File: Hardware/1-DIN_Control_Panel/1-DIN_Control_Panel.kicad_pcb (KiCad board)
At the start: 2 copper layers, 177.8 x 50.8 mm, 0 parts

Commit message: Schematic progress
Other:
- outline, holes or cut-outs redrawn
- board text added: "1"
- board text added: "2"
- board text added: "3"
- board text added: "4"
- board text added: "5"
- board text added: "6"
- board text added: "7"
- board text added: "AMP"
- board text added: "AUX JUMP"
- board text added: "BATT BYPASS"
- board text added: "BRT"
- board text added: "MASTER"
- board text added: "MODE"
- board text added: "OFF"
- board text added: "ON"
- board text added: "VOLT"

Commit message: Assigned footprints, expanded schematic
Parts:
- added A1: Arduino Nano, Module:Arduino_Nano, F.Cu at (-5.53, 52.9)
- added C1: 100nF, Capacitor_SMD:C_0603_1608Metric_Pad1.08x0.95mm_HandSolder, F.Cu at (-5.41, 107.6)
- added C2: 100nF, Capacitor_SMD:C_0603_1608Metric_Pad1.08x0.95mm_HandSolder, F.Cu at (-5.41, 110.2)
- added C3: 100nF, Capacitor_SMD:C_0603_1608Metric_Pad1.08x0.95mm_HandSolder, F.Cu at (-5.41, 112.7)
- added C4: 100nF, Capacitor_SMD:C_0603_1608Metric_Pad1.08x0.95mm_HandSolder, F.Cu at (-5.41, 115.2)
- added C5: DNP, Capacitor_SMD:C_0603_1608Metric_Pad1.08x0.95mm_HandSolder, F.Cu at (-5.41, 117.7)
- added C6: DNP, Capacitor_SMD:C_0603_1608Metric_Pad1.08x0.95mm_HandSolder, F.Cu at (-5.41, 120.2)
- added C7: 10µF, Capacitor_SMD:C_0603_1608Metric_Pad1.08x0.95mm_HandSolder, F.Cu at (-5.41, 122.7)
- added C8: 22µF, Capacitor_SMD:C_0603_1608Metric_Pad1.08x0.95mm_HandSolder, F.Cu at (-5.41, 125.2)
- added C9: 100nF, Capacitor_SMD:C_0603_1608Metric_Pad1.08x0.95mm_HandSolder, F.Cu at (-1.06, 107.6)
- added D1: D, Diode_THT:D_A-405_P2.54mm_Vertical_AnodeUp, F.Cu at (24.7, 58.7)
- added D2: D, Diode_THT:D_A-405_P2.54mm_Vertical_AnodeUp, F.Cu at (24.7, 62.9)
- added D3: D, Diode_THT:D_A-405_P2.54mm_Vertical_AnodeUp, F.Cu at (24.7, 67.2)
- added J1: 2x05 Molex Micro-Fit 3.0 43045, Connector_Molex:Molex_Micro-Fit_3.0_43045-1012_2x05_P3.00mm_Vertical, F.Cu at (16.4, 83.9)
- added J2: Pot/SW - Brightness, TerminalBlock:TerminalBlock_bornier-5_P5.08mm, F.Cu at (8.73, 122.7)
- added J3: SW - Aux Jump-Start, Connector_Molex:Molex_Micro-Fit_3.0_43045-0212_2x01_P3.00mm_Vertical, F.Cu at (-2.98, 99.0)
- added J4: SW - Battery Bypass, Connector_Molex:Molex_Micro-Fit_3.0_43045-0212_2x01_P3.00mm_Vertical, F.Cu at (6.23, 99.0)
- added J5: SW - Master Power, Connector_Molex:Molex_Micro-Fit_3.0_43045-0212_2x01_P3.00mm_Vertical, F.Cu at (15.4, 99.0)
- added K1: FINDER-40.52, Relay_THT:Relay_DPDT_Finder_30.22, F.Cu at (7.64, 116.0)
- added R1: DNP, Resistor_SMD:R_0603_1608Metric_Pad0.98x0.95mm_HandSolder, F.Cu at (-1.06, 110.2)
- added R10: 100kΩ, Resistor_SMD:R_0603_1608Metric_Pad0.98x0.95mm_HandSolder, F.Cu at (3.29, 112.7)
- added R11: 100kΩ, Resistor_SMD:R_0603_1608Metric_Pad0.98x0.95mm_HandSolder, F.Cu at (3.29, 115.2)
- added R12: 100kΩ, Resistor_SMD:R_0603_1608Metric_Pad0.98x0.95mm_HandSolder, F.Cu at (3.29, 117.7)
- added R2: DNP, Resistor_SMD:R_0603_1608Metric_Pad0.98x0.95mm_HandSolder, F.Cu at (-1.06, 112.7)
- added R3: 12kΩ, Resistor_SMD:R_0603_1608Metric_Pad0.98x0.95mm_HandSolder, F.Cu at (-1.06, 115.2)
- added R4: 22kΩ, Resistor_SMD:R_0603_1608Metric_Pad0.98x0.95mm_HandSolder, F.Cu at (-1.06, 117.7)
- added R5: 10kΩ, Resistor_SMD:R_0603_1608Metric_Pad0.98x0.95mm_HandSolder, F.Cu at (-1.06, 120.2)
- added R6: 100kΩ, Resistor_SMD:R_0603_1608Metric_Pad0.98x0.95mm_HandSolder, F.Cu at (-1.06, 122.7)
- added R7: 2.7kΩ, Resistor_SMD:R_0603_1608Metric_Pad0.98x0.95mm_HandSolder, F.Cu at (-1.06, 125.2)
- added R8: 100kΩ, Resistor_SMD:R_0603_1608Metric_Pad0.98x0.95mm_HandSolder, F.Cu at (3.29, 107.6)
- added R9: 100kΩ, Resistor_SMD:R_0603_1608Metric_Pad0.98x0.95mm_HandSolder, F.Cu at (3.29, 110.2)
- added RV1: 500Ω, Buzzer_Beeper:Buzzer_12x9.5RM7.6, F.Cu at (-48.7, 138.3)
- added U1: D198K, Display_7Segment:D1X8K, F.Cu at (-25.5, 50.2)
- added U2: D198K, Display_7Segment:D1X8K, F.Cu at (-25.5, 64.3)
- added U3: D198K, Display_7Segment:D1X8K, F.Cu at (-25.5, 78.3)
- added U4: D198K, Display_7Segment:D1X8K, F.Cu at (-25.5, 92.4)
- added U5: D198K, Display_7Segment:D1X8K, F.Cu at (-25.5, 106.4)
- added U6: D198K, Display_7Segment:D1X8K, F.Cu at (-25.5, 120.5)
- added U7: MAX7221xNG, Package_DIP:DIP-24_W7.62mm, F.Cu at (13.4, 50.4)
- added U8: LM324DR, Package_SO:SOIC-14_3.9x8.7mm_P1.27mm, F.Cu at (24.3, 100.7)
- added U9: AP1117-50, Package_TO_SOT_SMD:SOT-223-3_TabPin2, F.Cu at (27.5, 52.4)
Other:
- board size 177.8 x 50.8 mm -> 221.3 x 154.1 mm
- board text added: "PUSH TO TEST"

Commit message: Changed to 14-segement Characters
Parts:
- U7: footprint Package_DIP:DIP-24_W7.62mm -> Package_DIP:DIP-24_W8.89mm_SMDSocket_LongPads
- moved A1 54.2 mm to (48.2, 59.9)
- moved U7 15.1 mm to (17.7, 64.8)
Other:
- board size 221.3 x 154.1 mm -> 177.8 x 130.7 mm

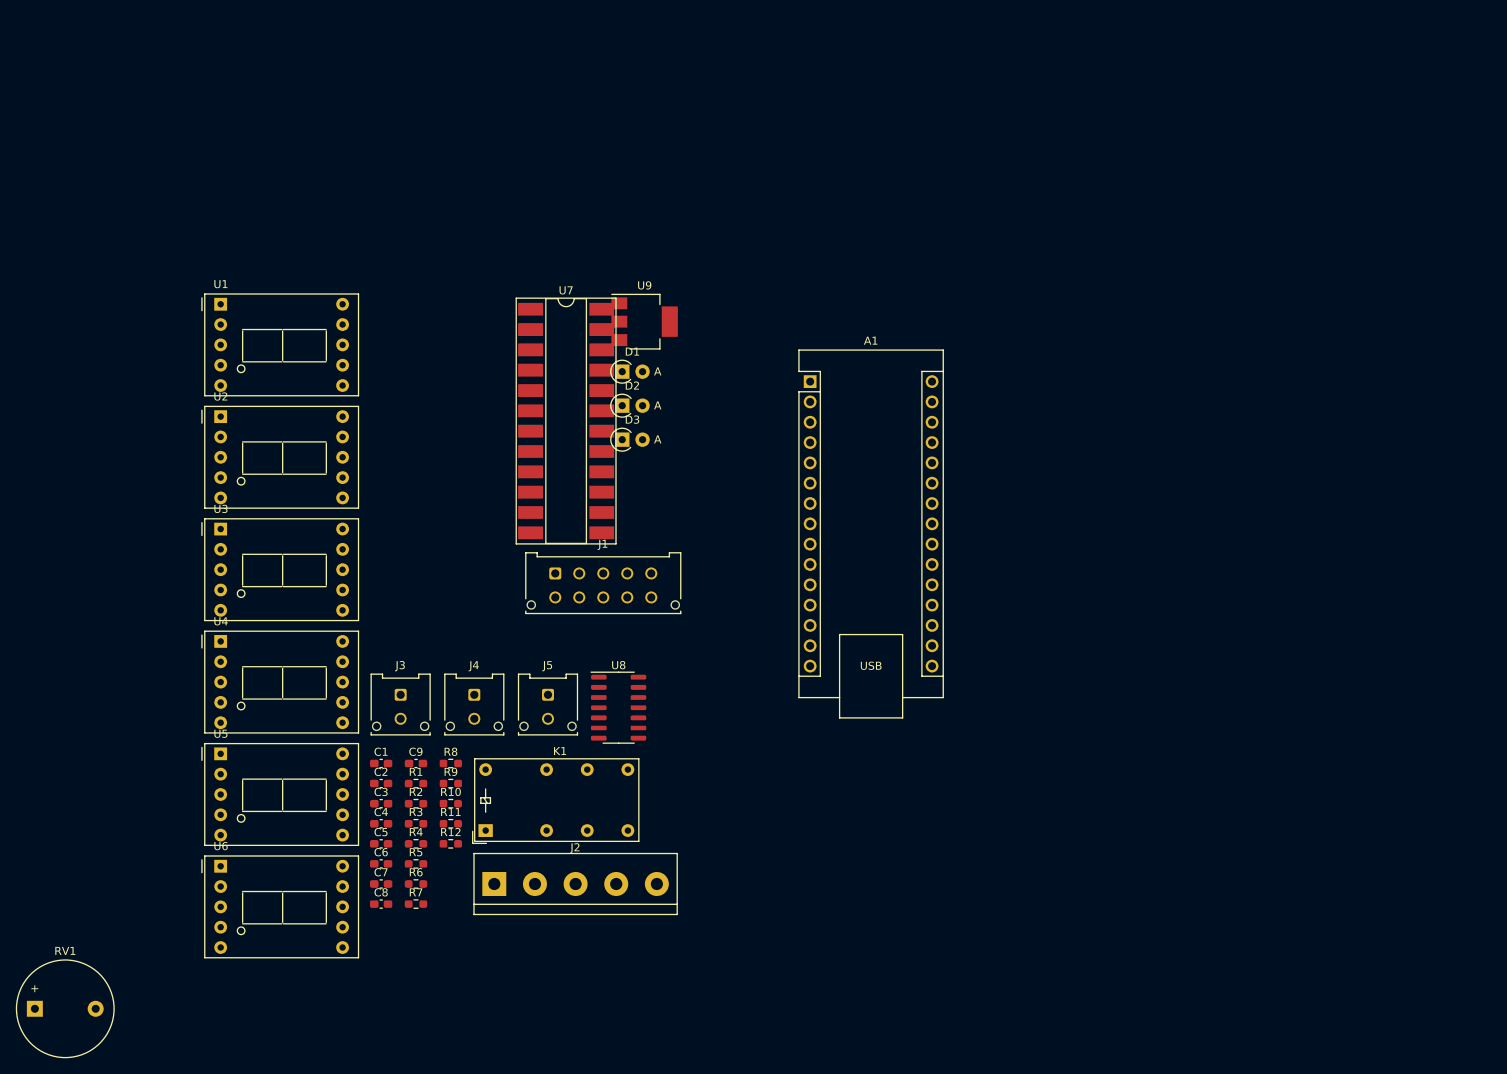
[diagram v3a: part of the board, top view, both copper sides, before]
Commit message: Added footprints to pcb file
Need a proper footprint for the 14-seg LEDs, MAX driver chips...and something else that I can't remember right now
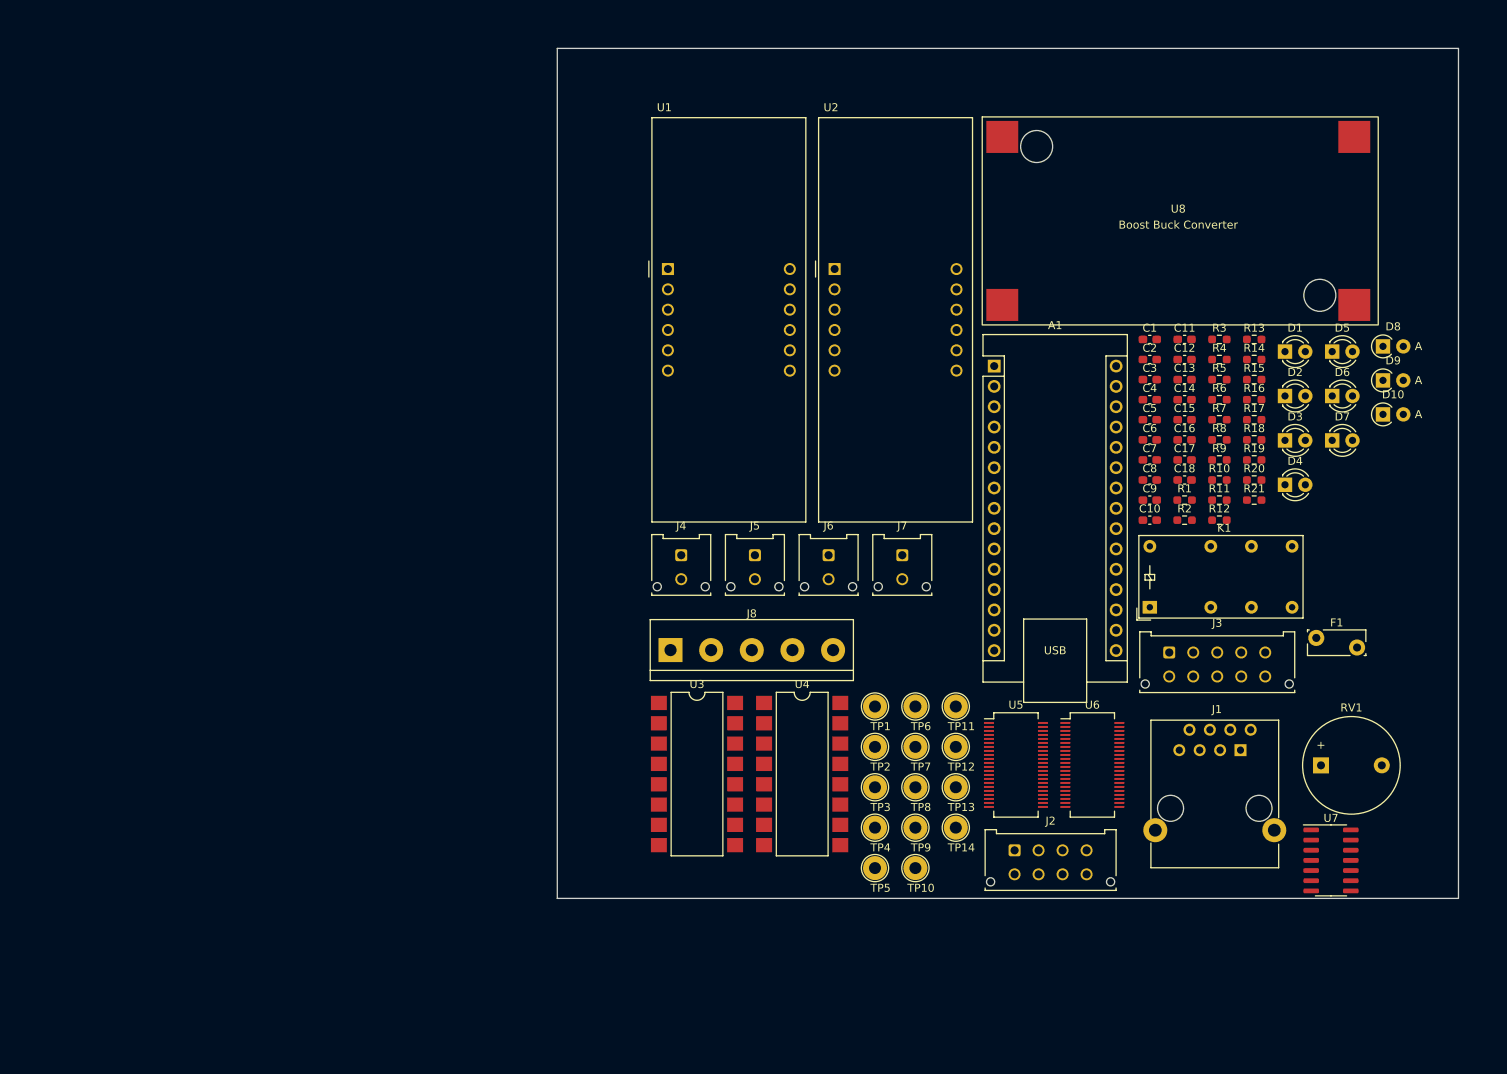
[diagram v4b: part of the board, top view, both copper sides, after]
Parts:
- removed U9: AP1117-50, Package_TO_SOT_SMD:SOT-223-3_TabPin2
- added C10: 100nF, Capacitor_SMD:C_0603_1608Metric_Pad1.08x0.95mm_HandSolder, F.Cu at (90.7, 77.2)
- added C11: 100nF, Capacitor_SMD:C_0603_1608Metric_Pad1.08x0.95mm_HandSolder, F.Cu at (95.0, 54.6)
- added C12: 100nF, Capacitor_SMD:C_0603_1608Metric_Pad1.08x0.95mm_HandSolder, F.Cu at (95.0, 57.1)
- added C13: 100nF, Capacitor_SMD:C_0603_1608Metric_Pad1.08x0.95mm_HandSolder, F.Cu at (95.0, 59.6)
- added C14: 100nF, Capacitor_SMD:C_0603_1608Metric_Pad1.08x0.95mm_HandSolder, F.Cu at (95.0, 62.2)
- added C15: 10µF, Capacitor_SMD:C_0603_1608Metric_Pad1.08x0.95mm_HandSolder, F.Cu at (95.0, 64.7)
- added C16: DNP, Capacitor_SMD:C_0603_1608Metric_Pad1.08x0.95mm_HandSolder, F.Cu at (95.0, 67.2)
- added C17: DNP, Capacitor_SMD:C_0603_1608Metric_Pad1.08x0.95mm_HandSolder, F.Cu at (95.0, 69.7)
- added C18: 22µF, Capacitor_SMD:C_0603_1608Metric_Pad1.08x0.95mm_HandSolder, F.Cu at (95.0, 72.2)
- added D10: D, Diode_THT:D_A-405_P2.54mm_Vertical_AnodeUp, F.Cu at (119.8, 64.0)
- added D4: LED_Filled, LED_THT:LED_D3.0mm, F.Cu at (107.6, 72.8)
- added D5: LED_Filled, LED_THT:LED_D3.0mm, F.Cu at (113.5, 56.1)
- added D6: LED_Filled, LED_THT:LED_D3.0mm, F.Cu at (113.5, 61.7)
- added D7: LED_Filled, LED_THT:LED_D3.0mm, F.Cu at (113.5, 67.2)
- added D8: D, Diode_THT:D_A-405_P2.54mm_Vertical_AnodeUp, F.Cu at (119.8, 55.5)
- added D9: D, Diode_THT:D_A-405_P2.54mm_Vertical_AnodeUp, F.Cu at (119.8, 59.8)
- added F1: 1A Trip, Fuse:Fuse_Bourns_MF-RG300, F.Cu at (111.5, 91.9)
- added J6: SW - Battery Bypass, Connector_Molex:Molex_Micro-Fit_3.0_43045-0212_2x01_P3.00mm_Vertical, F.Cu at (50.5, 81.6)
- added J7: SW - Master Power, Connector_Molex:Molex_Micro-Fit_3.0_43045-0212_2x01_P3.00mm_Vertical, F.Cu at (59.7, 81.6)
- added J8: Pot/SW - Brightness, TerminalBlock:TerminalBlock_bornier-5_P5.08mm, F.Cu at (30.8, 93.5)
- added R13: 10kΩ, Resistor_SMD:R_0603_1608Metric_Pad0.98x0.95mm_HandSolder, F.Cu at (103.7, 54.6)
- added R14: 100kΩ, Resistor_SMD:R_0603_1608Metric_Pad0.98x0.95mm_HandSolder, F.Cu at (103.7, 57.1)
- added R15: 2.7kΩ, Resistor_SMD:R_0603_1608Metric_Pad0.98x0.95mm_HandSolder, F.Cu at (103.7, 59.6)
- added R16: 100kΩ, Resistor_SMD:R_0603_1608Metric_Pad0.98x0.95mm_HandSolder, F.Cu at (103.7, 62.2)
- added R17: 100kΩ, Resistor_SMD:R_0603_1608Metric_Pad0.98x0.95mm_HandSolder, F.Cu at (103.7, 64.7)
- added R18: 100kΩ, Resistor_SMD:R_0603_1608Metric_Pad0.98x0.95mm_HandSolder, F.Cu at (103.7, 67.2)
- added R19: 100kΩ, Resistor_SMD:R_0603_1608Metric_Pad0.98x0.95mm_HandSolder, F.Cu at (103.7, 69.7)
- added R20: 100kΩ, Resistor_SMD:R_0603_1608Metric_Pad0.98x0.95mm_HandSolder, F.Cu at (103.7, 72.2)
- added R21: 0Ω or Bridge, Resistor_SMD:R_0603_1608Metric_Pad0.98x0.95mm_HandSolder, F.Cu at (103.7, 74.7)
- added TP1: TestPoint_Flag, TestPoint:TestPoint_Loop_D2.54mm_Drill1.5mm_Beaded, F.Cu at (56.3, 100.5)
- added TP10: TestPoint_Flag, TestPoint:TestPoint_Loop_D2.54mm_Drill1.5mm_Beaded, F.Cu at (61.4, 120.7)
- added TP11: TestPoint_Flag, TestPoint:TestPoint_Loop_D2.54mm_Drill1.5mm_Beaded, F.Cu at (66.4, 100.5)
- added TP12: TestPoint_Flag, TestPoint:TestPoint_Loop_D2.54mm_Drill1.5mm_Beaded, F.Cu at (66.4, 105.6)
- added TP13: TestPoint_Flag, TestPoint:TestPoint_Loop_D2.54mm_Drill1.5mm_Beaded, F.Cu at (66.4, 110.6)
- added TP14: TestPoint_Flag, TestPoint:TestPoint_Loop_D2.54mm_Drill1.5mm_Beaded, F.Cu at (66.4, 115.7)
- added TP2: TestPoint_Flag, TestPoint:TestPoint_Loop_D2.54mm_Drill1.5mm_Beaded, F.Cu at (56.3, 105.6)
- added TP3: TestPoint_Flag, TestPoint:TestPoint_Loop_D2.54mm_Drill1.5mm_Beaded, F.Cu at (56.3, 110.6)
- added TP4: TestPoint_Flag, TestPoint:TestPoint_Loop_D2.54mm_Drill1.5mm_Beaded, F.Cu at (56.3, 115.7)
- added TP5: TestPoint_Flag, TestPoint:TestPoint_Loop_D2.54mm_Drill1.5mm_Beaded, F.Cu at (56.3, 120.7)
- added TP6: TestPoint_Flag, TestPoint:TestPoint_Loop_D2.54mm_Drill1.5mm_Beaded, F.Cu at (61.4, 100.5)
- added TP7: TestPoint_Flag, TestPoint:TestPoint_Loop_D2.54mm_Drill1.5mm_Beaded, F.Cu at (61.4, 105.6)
- added TP8: TestPoint_Flag, TestPoint:TestPoint_Loop_D2.54mm_Drill1.5mm_Beaded, F.Cu at (61.4, 110.6)
- added TP9: TestPoint_Flag, TestPoint:TestPoint_Loop_D2.54mm_Drill1.5mm_Beaded, F.Cu at (61.4, 115.7)
- C1, C2: value 100nF -> 47µF
- C5, C6: value DNP -> 100nF
- C7: value 10µF -> 22pF
- C8: value 22µF -> 22pF
- D1, D2, D3: value D -> LED_Filled; footprint Diode_THT:D_A-405_P2.54mm_Vertical_AnodeUp -> LED_THT:LED_D3.0mm
- J1: value 2x05 Molex Micro-Fit 3.0 43045 -> Selector Knob Connector; footprint Connector_Molex:Molex_Micro-Fit_3.0_43045-1012_2x05_P3.00mm_Vertical -> libraries:Mystery_RJ45
- J2: value Pot/SW - Brightness -> Rotary Switch 1x7; footprint TerminalBlock:TerminalBlock_bornier-5_P5.08mm -> Connector_Molex:Molex_Micro-Fit_3.0_43045-0812_2x04_P3.00mm_Vertical
- J3: value SW - Aux Jump-Start -> 2x05 Molex Micro-Fit 3.0 43045; footprint Connector_Molex:Molex_Micro-Fit_3.0_43045-0212_2x01_P3.00mm_Vertical -> Connector_Molex:Molex_Micro-Fit_3.0_43045-1012_2x05_P3.00mm_Vertical
- J4: value SW - Battery Bypass -> UART Expansion
- J5: value SW - Master Power -> SW - Aux Jump-Start
- R1: value DNP -> 10kΩ
- R10, R9: value 100kΩ -> 56kΩ
- R11: value 100kΩ -> 10kΩ
- R12: value 100kΩ -> 22kΩ
- R2: value DNP -> 150Ω
- R3: value 12kΩ -> 150Ω
- R4: value 22kΩ -> 150Ω
- R5: value 10kΩ -> 150Ω
- R6, R8: value 100kΩ -> 150Ω
- R7: value 2.7kΩ -> 150Ω
- U1, U2: value D198K -> CA56-12SEKWA; footprint Display_7Segment:D1X8K -> Display_7Segment:CA56-12SEKWA
- U3, U4: value D198K -> LTV-847S; footprint Display_7Segment:D1X8K -> Package_DIP:SMDIP-16_W9.53mm
- U5, U6: value D198K -> MAX 6954 - SSOP; footprint Display_7Segment:D1X8K -> Package_SO:SSOP-44_5.3x12.8mm_P0.5mm
- U7: value MAX7221xNG -> LM324DR; footprint Package_DIP:DIP-24_W8.89mm_SMDSocket_LongPads -> Package_SO:SOIC-14_3.9x8.7mm_P1.27mm
- U8: value LM324DR -> 12V->5V Variable Boost Buck Converter; footprint Package_SO:SOIC-14_3.9x8.7mm_P1.27mm -> libraries:BoostBuck
- moved RV1 163.6 mm to (112.1, 107.9)
- moved R3 117.3 mm to (99.4, 54.6)
- moved R4 117.3 mm to (99.4, 57.1)
- moved R5 117.3 mm to (99.4, 59.6)
- moved R6 117.3 mm to (99.4, 62.2)
- moved R7 117.3 mm to (99.4, 64.7)
- moved U7 110.3 mm to (113.3, 119.8)
- moved C1 109.7 mm to (90.7, 54.6)
- moved C2 109.7 mm to (90.7, 57.1)
- moved C3 109.7 mm to (90.7, 59.6)
- moved C4 109.7 mm to (90.7, 62.2)
- moved C5 109.7 mm to (90.7, 64.7)
- moved C6 109.7 mm to (90.7, 67.2)
- moved C7 109.7 mm to (90.7, 69.7)
- moved C8 109.7 mm to (90.7, 72.2)
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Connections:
- A1 pad 1: unconnected-(A1-D1/TX-Pad1) -> /TX-EXPANSION
- A1 pad 12: unconnected-(A1-D9-Pad12) -> /Arduino_~{CS}_VOLT
- A1 pad 13: unconnected-(A1-D10-Pad13) -> /Arduino_~{CS}_AMP
- A1 pad 14: /MOSI -> /Arduino_MOSI
- A1 pad 15: /CS -> /Arduino_MISO
- A1 pad 16: /CLK -> /Arduino_SCK
- A1 pad 19: /VOLTAGE_SENSE -> /BRIGHTNESS_CONTROL
- A1 pad 2: unconnected-(A1-D0/RX-Pad2) -> /RX-EXPANSION
- A1 pad 20: unconnected-(A1-A1-Pad20) -> /VOLTAGE_SENSE
- A1 pad 27: unconnected-(A1-+5V-Pad27) -> +5V
- A1 pad 30: VCC -> unconnected-(A1-VIN-Pad30)
- A1 pad 6: unconnected-(A1-D3-Pad6) -> /MODE_LED_BRIGHTNESS
- A1 pad 7: unconnected-(A1-D4-Pad7) -> /MODE_PWR_DETECT
- C1 pad 1: Net-(J2-A) -> Net-(C1-Pad1)
- C2 pad 1: /SHUNT+ -> Net-(C2-Pad1)
- C3 pad 1: /SHUNT- -> Net-(C1-Pad1)
- C4 pad 1: /VOLTAGE_SENSE -> Net-(C2-Pad1)
- C5 pad 1: Net-(U8A--) -> Net-(C1-Pad1)
- C6 pad 1: Net-(U8A-+) -> Net-(C2-Pad1)
- C7 pad 1: VCC -> Net-(U5-OSC)
- C8 pad 1: +5V -> Net-(U6-OSC)
- C9 pad 1: /CURRENT_SENSE -> /VOLTAGE_SENSE
- D1 pad 1: /CONTACTOR_COIL -> /MODE_1_LED
- D1 pad 2: /12V_ON -> Net-(D1-A)
- D2 pad 1: Net-(D2-K) -> /MODE_2_LED
- D2 pad 2: /SHUNT+ -> Net-(D2-A)
- D3 pad 1: /BATT_RAW -> /MODE_3_LED
- J1 pad 1: GND -> /MODE_1_OUT
- J1 pad 2: /SHUNT+ -> /MODE_2_OUT
- J1 pad 3: /SHUNT- -> /MODE_3_OUT
- J1 pad 4: /CONTACTOR_COIL -> /MODE_4_OUT
- J1 pad 5: /12V_ON -> /MODE_5_OUT
- J1 pad 6: /MASTER_OPEN -> /MODE_6_OUT
- J1 pad 7: /MASTER_COMMON -> /MODE_7_OUT
- J1 pad 8: /BATT_BYPASS -> /MODE_12V_OUT
- J2 pad 1: Net-(J2-A) -> /MODE_1
- J2 pad 2: +5V -> /MODE_2
- J2 pad 3: unconnected-(J2-B-Pad3) -> /MODE_3
- J2 pad 4: GND -> /MODE_4
- J2 pad 5: Net-(D3-A) -> /MODE_5
- J3 pad 1: /CONTACTOR_COIL -> GND
- J3 pad 2: Net-(D2-K) -> /SHUNT+
- J4 pad 1: /SHUNT+ -> /RX-EXPANSION
- J4 pad 2: /BATT_BYPASS -> /TX-EXPANSION
- J5 pad 1: /MASTER_OPEN -> /CONTACTOR_COIL
- J5 pad 2: /MASTER_COMMON -> Net-(D9-K)
- K1 pad 11: VCC -> Net-(F1-Pad1)
- K1 pad A2: Net-(D3-A) -> /VOLT_SOURCE_SELECT
- R1 pad 1: +5V -> GND
- R1 pad 2: /CS -> /MODE_PWR_DETECT
- R10 pad 1: Net-(R10-Pad1) -> GND
- R10 pad 2: Net-(U8A-+) -> Net-(U6-ISET)
- R11 pad 1: Net-(U8A--) -> GND
- R11 pad 2: /CURRENT_SENSE -> Net-(J8-B)
- R12 pad 1: Net-(U8A-+) -> /VOLTAGE_SENSE
- R12 pad 2: GND -> VCC
- R2 pad 1: /CS -> Net-(R2-Pad1)
- R2 pad 2: GND -> Net-(D1-A)
- R3 pad 1: Net-(U7-ISET) -> Net-(R2-Pad1)
- R3 pad 2: Net-(J2-A) -> Net-(D2-A)
- R4 pad 1: /VOLTAGE_SENSE -> Net-(R2-Pad1)
- R4 pad 2: VCC -> Net-(D3-A)
- R5 pad 1: GND -> Net-(R2-Pad1)
- R5 pad 2: /VOLTAGE_SENSE -> Net-(D4-A)
- R6 pad 1: Net-(U8B--) -> Net-(R2-Pad1)
- R6 pad 2: Net-(R6-Pad2) -> Net-(D5-A)
- R7 pad 1: Net-(R7-Pad1) -> Net-(R2-Pad1)
- R7 pad 2: Net-(U8B--) -> Net-(D6-A)
- R8 pad 1: Net-(R10-Pad1) -> Net-(R2-Pad1)
- R8 pad 2: Net-(U8C--) -> Net-(D7-A)
- R9 pad 1: Net-(R6-Pad2) -> GND
- R9 pad 2: Net-(U8A--) -> Net-(U5-ISET)
- RV1 pad 1: Net-(R7-Pad1) -> Net-(R15-Pad1)
- RV1 pad 2: Net-(U8C--) -> Net-(U7C--)
- U1 pad 1: /SEG_E -> /DIGIT1_G2-N_ANODE
- U1 pad 10: /SEG_G -> /DIGIT3_G2-N_ANODE
- U1 pad 2: /SEG_D -> /DIGIT2_G2-N_ANODE
- U1 pad 3: /VOLT_100 -> /D_CATHODE
- U1 pad 4: /SEG_C -> /C_CATHODE
- U1 pad 5: /SEG_DP -> /G_CATHODE
- U1 pad 6: /SEG_B -> /E_CATHODE
- U1 pad 7: /SEG_A -> /COLON_DP_ANODE
- U1 pad 8: /VOLT_100 -> /DIGIT4_A-G1_ANODE
- U1 pad 9: /SEG_F -> /DIGIT4_G2-N_ANODE
- U2 pad 1: /SEG_E -> /DIGIT1_G2-N_ANODE
- U2 pad 10: /SEG_G -> /DIGIT3_G2-N_ANODE
- U2 pad 2: /SEG_D -> /DIGIT2_G2-N_ANODE
- U2 pad 3: /VOLT_10 -> /D_CATHODE
- U2 pad 4: /SEG_C -> /C_CATHODE
- U2 pad 5: /SEG_DP -> /G_CATHODE
- U2 pad 6: /SEG_B -> /E_CATHODE
- U2 pad 7: /SEG_A -> /COLON_DP_ANODE
- U2 pad 8: /VOLT_10 -> /DIGIT4_A-G1_ANODE
- U2 pad 9: /SEG_F -> /DIGIT4_G2-N_ANODE
- U3 pad 1: /SEG_E -> /MODE_1
- U3 pad 10: /SEG_G -> /MODE_4_LED
- U3 pad 2: /SEG_D -> /MODE_1_OUT
- U3 pad 3: /VOLT_1 -> /MODE_2
- U3 pad 4: /SEG_C -> /MODE_2_OUT
- U3 pad 5: /SEG_DP -> /MODE_3
- U3 pad 6: /SEG_B -> /MODE_3_OUT
- U3 pad 7: /SEG_A -> /MODE_4
- U3 pad 8: /VOLT_1 -> /MODE_4_OUT
- U3 pad 9: /SEG_F -> GND
- U4 pad 1: /SEG_E -> /MODE_5
- U4 pad 10: /SEG_G -> +5V
- U4 pad 2: /SEG_D -> /MODE_5_OUT
- U4 pad 3: /AMP_100 -> /MODE_6
- U4 pad 4: /SEG_C -> /MODE_6_OUT
- U4 pad 5: /SEG_DP -> /MODE_7
- U4 pad 6: /SEG_B -> /MODE_7_OUT
- U4 pad 7: /SEG_A -> /MODE_12V_OUT
- U4 pad 8: /AMP_100 -> /MODE_12V
- U4 pad 9: /SEG_F -> /MODE_PWR_DETECT
- U5 pad 1: /SEG_E -> Net-(U5-P0)
- U5 pad 10: /SEG_G -> /DIGIT2_G2-N_ANODE
- U5 pad 2: /SEG_D -> Net-(U5-P1)
- U5 pad 3: /AMP_10 -> /Arduino_~{CS}_VOLT
- U5 pad 4: /SEG_C -> /Arduino_MISO
- U5 pad 5: /SEG_DP -> /Arduino_SCK
- U5 pad 6: /SEG_B -> /Arduino_MOSI
- U5 pad 7: /SEG_A -> /DIGIT1_A-G1_ANODE
- U5 pad 8: /AMP_10 -> /DIGIT1_G2-N_ANODE
- U5 pad 9: /SEG_F -> /DIGIT2_A-G1_ANODE
- U6 pad 1: /SEG_E -> Net-(U6-P0)
- U6 pad 10: /SEG_G -> /DIGIT2_G2-N_ANODE
- U6 pad 2: /SEG_D -> Net-(U6-P1)
- U6 pad 3: /AMP_1 -> /Arduino_~{CS}_AMP
- U6 pad 4: /SEG_C -> /Arduino_MISO
- U6 pad 5: /SEG_DP -> /Arduino_SCK
- U6 pad 6: /SEG_B -> /Arduino_MOSI
- U6 pad 7: /SEG_A -> /DIGIT1_A-G1_ANODE
- U6 pad 8: /AMP_1 -> /DIGIT1_G2-N_ANODE
- U6 pad 9: /SEG_F -> /DIGIT2_A-G1_ANODE
- U7 pad 1: /MOSI -> /CURRENT_SENSE
- U7 pad 10: /AMP_1 -> /SHUNT-
- U7 pad 11: /VOLT_10 -> GND
- U7 pad 12: /CS -> unconnected-(U7D-+-Pad12)
- U7 pad 13: /CLK -> unconnected-(U7D---Pad13)
- U7 pad 14: /SEG_A -> unconnected-(U7-Pad14)
- U7 pad 2: /VOLT_100 -> Net-(U7A--)
- U7 pad 3: /AMP_10 -> Net-(U7A-+)
- U7 pad 4: GND -> +5V
- U7 pad 5: unconnected-(U7-DIG_6-Pad5) -> /SHUNT+
- U7 pad 6: /VOLT_1 -> Net-(U7B--)
- U7 pad 7: /AMP_100 -> Net-(R14-Pad2)
- U7 pad 8: unconnected-(U7-DIG_7-Pad8) -> Net-(R16-Pad1)
- U7 pad 9: GND -> Net-(U7C--)
- U8 pad 1: /CURRENT_SENSE -> VCC
- U8 pad 2: Net-(U8A--) -> GND
- U8 pad 3: Net-(U8A-+) -> +5V
- U8 pad 4: +5V -> GND
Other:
- board size 177.8 x 130.7 mm -> 177.8 x 255.2 mm
